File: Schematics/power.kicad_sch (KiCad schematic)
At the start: 7 parts, among them U5 AMS1117-3.3

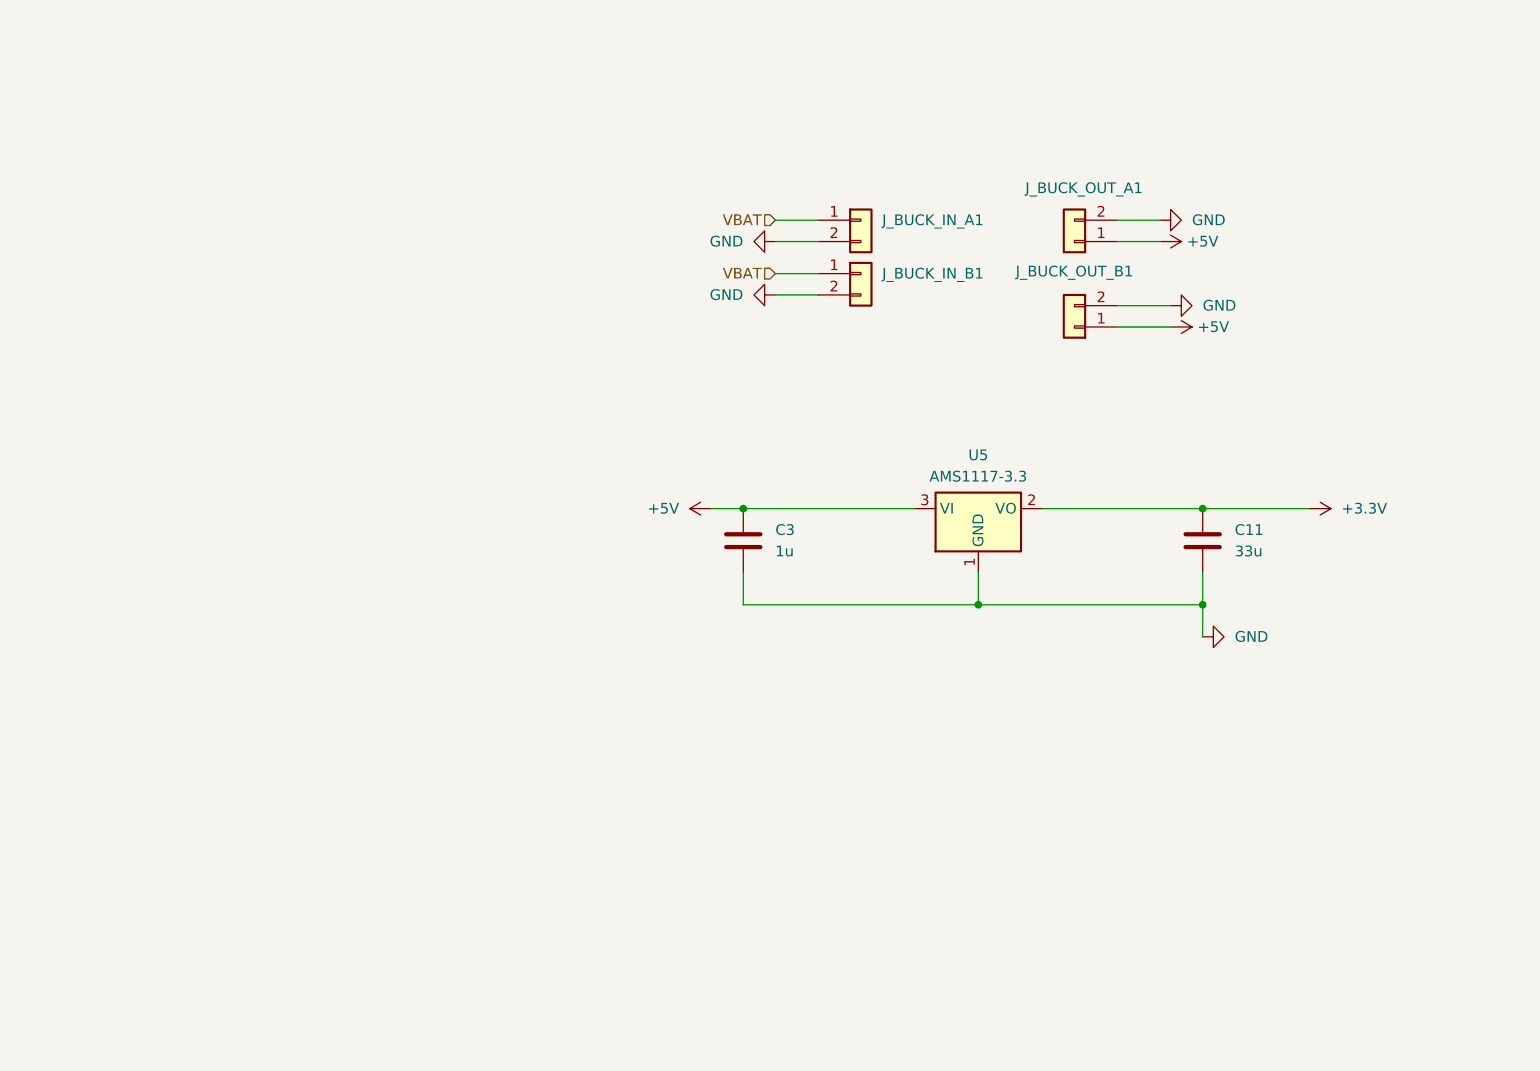
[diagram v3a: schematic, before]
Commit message: all nets are correct within PCB and correct CAN is implemented
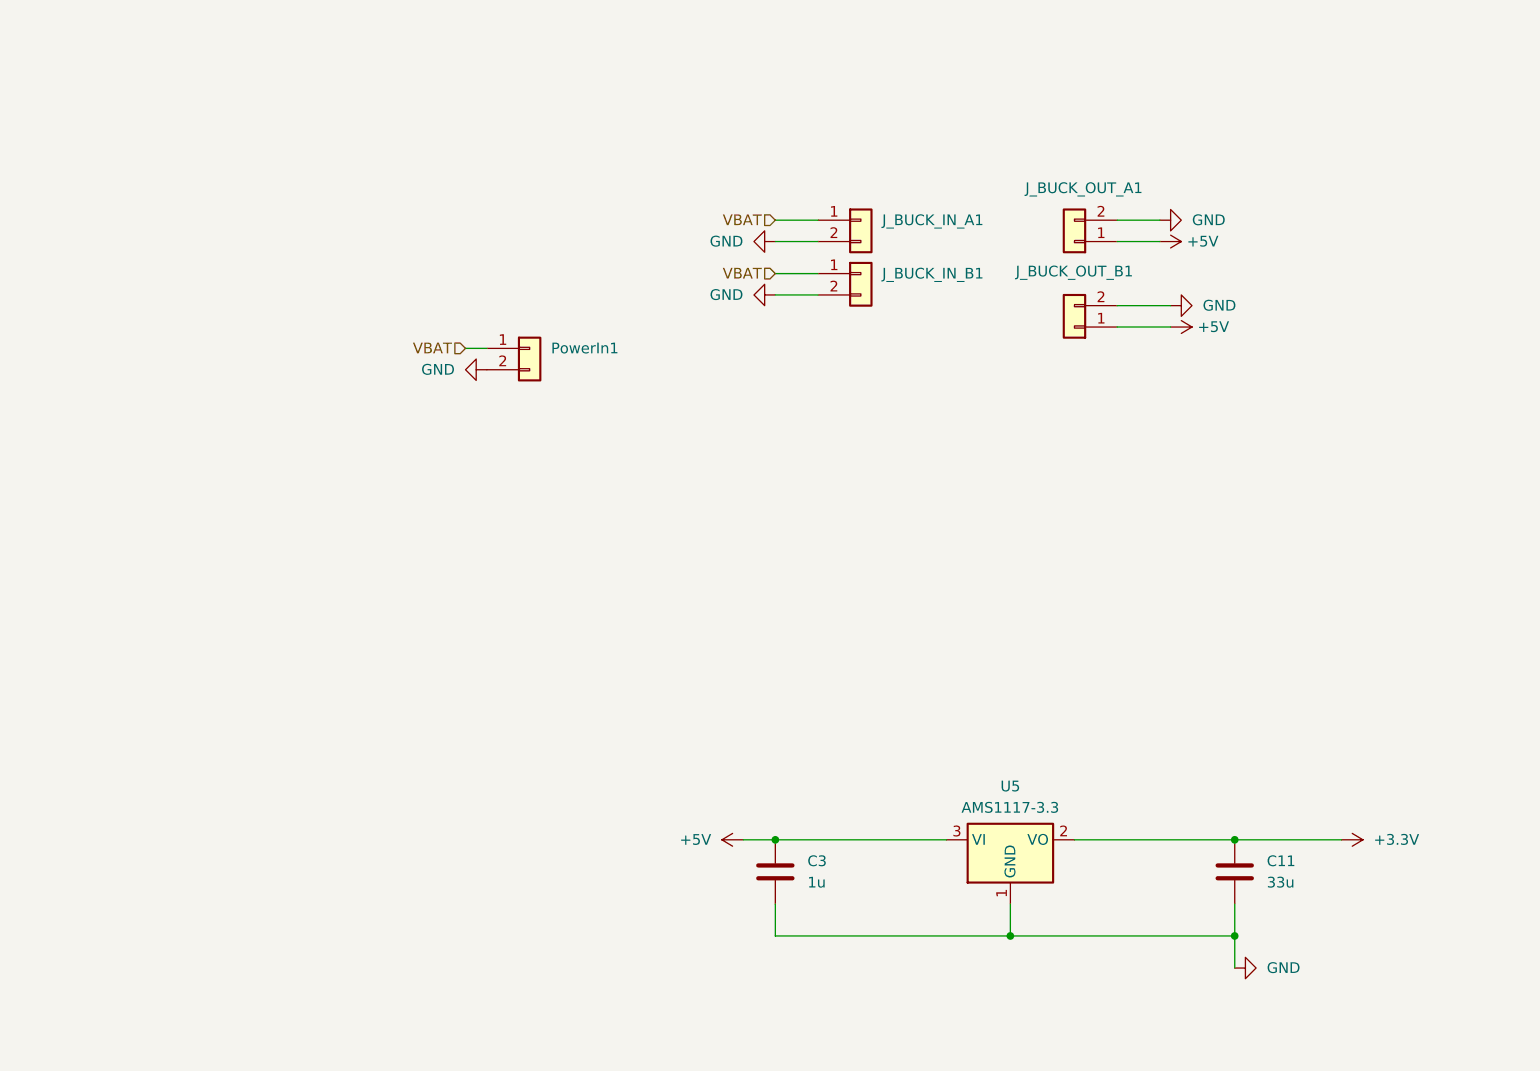
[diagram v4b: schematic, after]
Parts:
- added PowerIn1: ~, myFootprints:MOLEX_26013114, symbol Connector_Generic:Conn_01x02
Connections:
- net GND: now also PowerIn1.2 (Pin_2)
- net VBAT: now also PowerIn1.1 (Pin_1)
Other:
- moved on the sheet: C11, C3, U5

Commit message: Cleaned up schematic added ocilator added jtag 10 pin begining routing again
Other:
- moved on the sheet: C11, C3, J_BUCK_IN_A1, J_BUCK_IN_B1, J_BUCK_OUT_A1, J_BUCK_OUT_B1, PowerIn1, U5

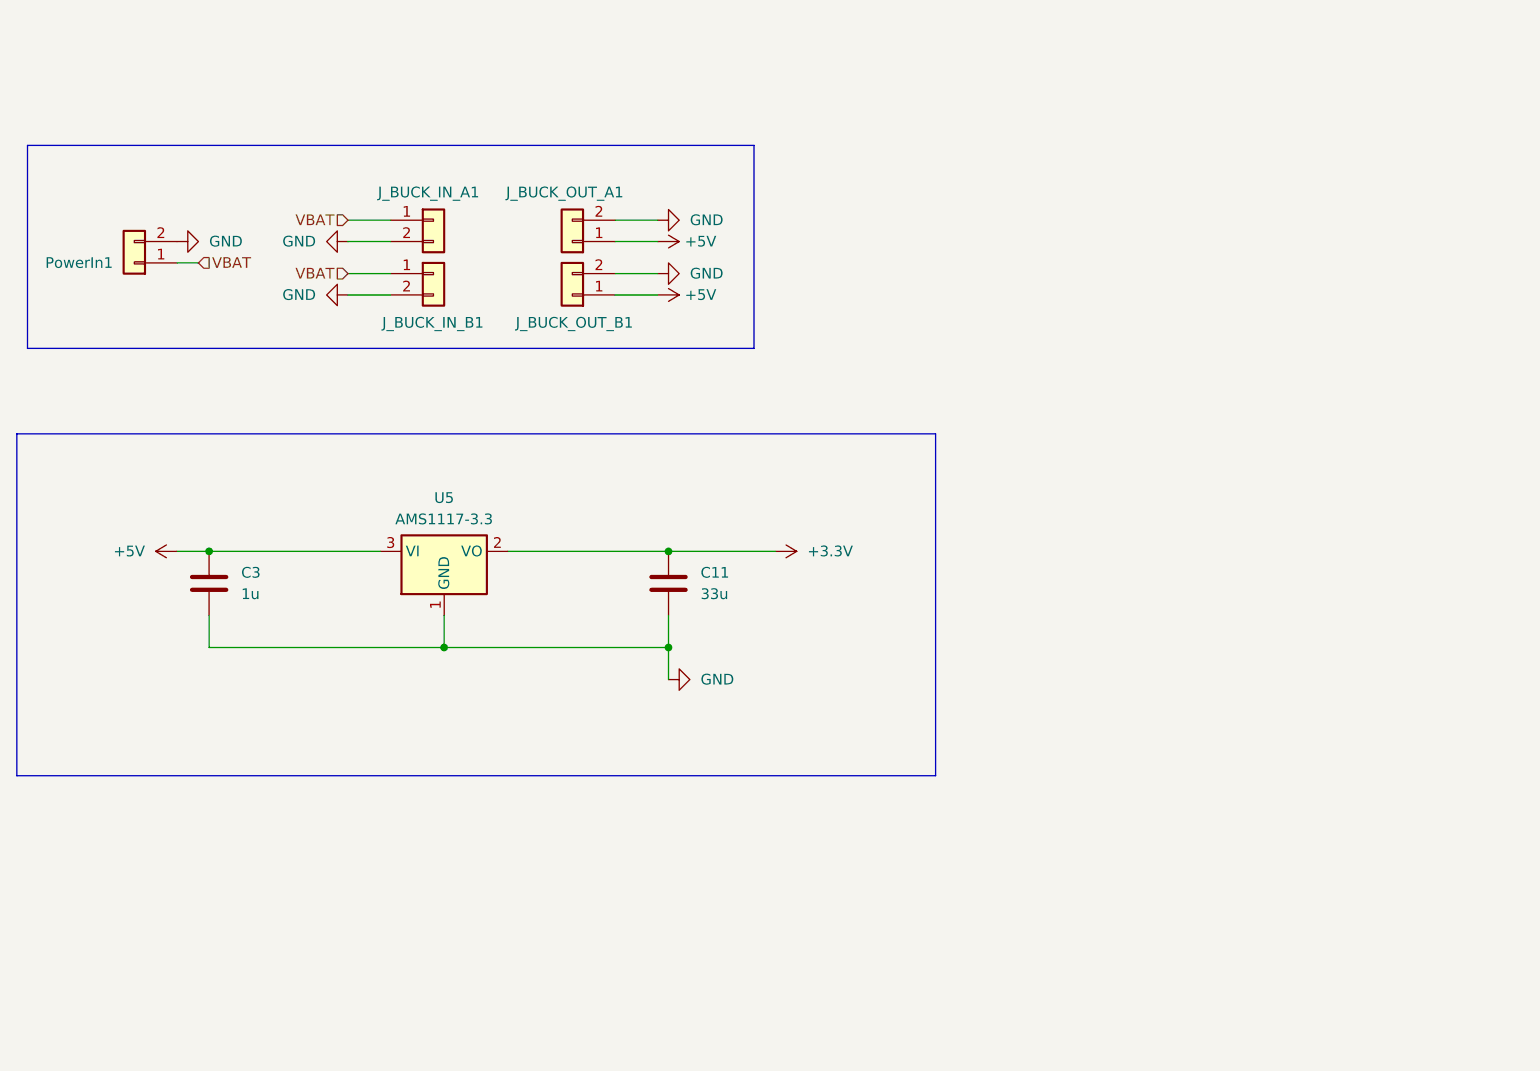
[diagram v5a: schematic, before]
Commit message: added LCSC numbers and generated BOM, fixed schematic
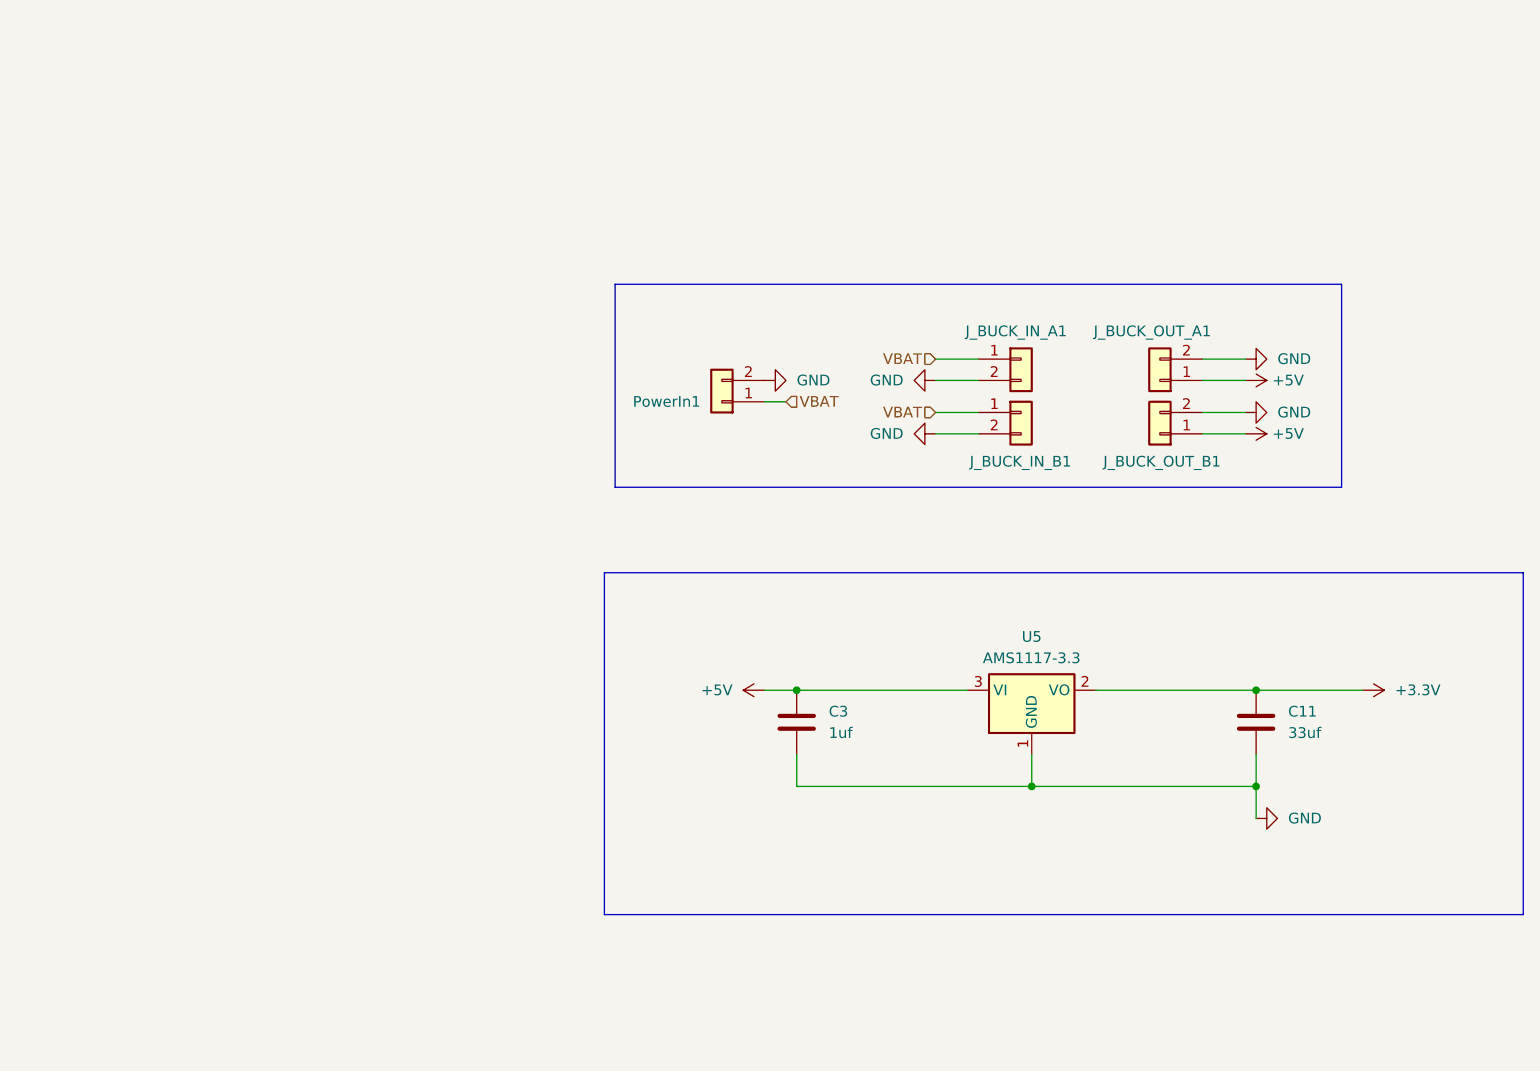
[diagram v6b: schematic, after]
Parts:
- C11: value 33u -> 33uf; LCSC (none) -> C432920
- C3: value 1u -> 1uf; LCSC (none) -> C28323
- J_BUCK_IN_A1, J_BUCK_IN_B1, J_BUCK_OUT_A1, J_BUCK_OUT_B1: now left out of the parts list
- PowerIn1: value ~ -> 2 pin Molex; LCSC (none) -> C17644051
- U5: LCSC (none) -> C6186
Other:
- moved on the sheet: C11, C3, J_BUCK_IN_A1, J_BUCK_IN_B1, J_BUCK_OUT_A1, J_BUCK_OUT_B1, PowerIn1, U5

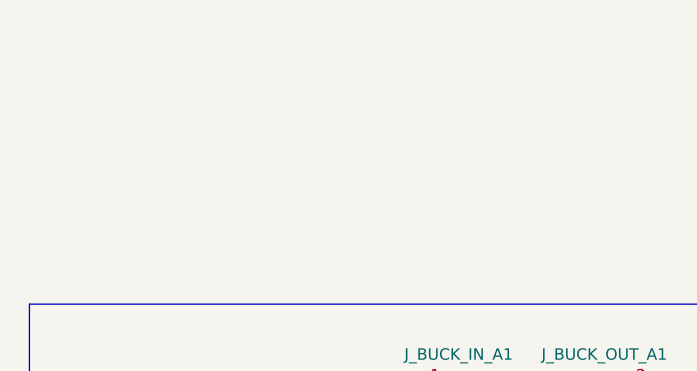
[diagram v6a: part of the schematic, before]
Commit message: Ran ERC added Pwr Flags
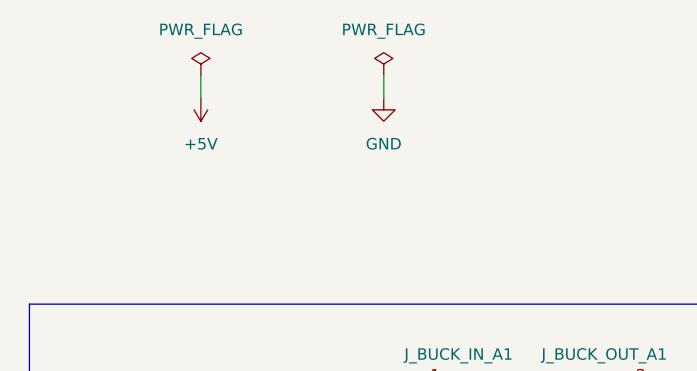
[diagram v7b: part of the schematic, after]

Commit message: final design pcb
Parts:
- removed C11: 33uf, Capacitor_SMD:C_0805_2012Metric_Pad1.18x1.45mm_HandSolder, symbol Device:C
- removed C3: 1uf, Capacitor_SMD:C_0805_2012Metric_Pad1.18x1.45mm_HandSolder, symbol Device:C
- removed U5: AMS1117-3.3, Package_TO_SOT_SMD:SOT-223-3_TabPin2, symbol Regulator_Linear:AMS1117-3.3
- added C16: 1u, Capacitor_SMD:C_0805_2012Metric_Pad1.18x1.45mm_HandSolder, symbol Device:C
- added C17: 4.7u, Capacitor_SMD:C_0805_2012Metric_Pad1.18x1.45mm_HandSolder, symbol Device:C
- added D2, D3: D_Schottky, Diode_SMD:D_2114_3652Metric, symbol Device:D_Schottky
- added U2: LDL1117-3.3, myFootprints:SOT230P700X180-4N, symbol Footprints:LDL1117-3.3
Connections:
- net +3.3V: now also C17.1, U2.3 (Vout), U2.4 (Vout)
- net +5V: now also J_BUCK_OUT_B1.2 (Pin_2); no longer J_BUCK_OUT_A1.1 (Pin_1)
- net GND: now also J_BUCK_IN_A1.1 (Pin_1), J_BUCK_OUT_A1.1 (Pin_1), C16.2, C17.2, U2.2 (GND); no longer J_BUCK_IN_B1.2 (Pin_2), J_BUCK_OUT_B1.2 (Pin_2)
- net VBAT renamed +BATT
- net +BATT: now also J_BUCK_IN_B1.2 (Pin_2), D2.2 (A); no longer J_BUCK_IN_A1.1 (Pin_1)
- new net: C16.1, D2.1 (K), D3.1 (K), U2.1 (Vin)
- new net USB 5v: D3.2 (A)
